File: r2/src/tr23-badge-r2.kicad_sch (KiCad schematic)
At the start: 60 parts, among them Q1 MMBT3904-TP, Q2 MMBT3904-TP, Q3 MMBT3904-TP, Y1 32.768kHz

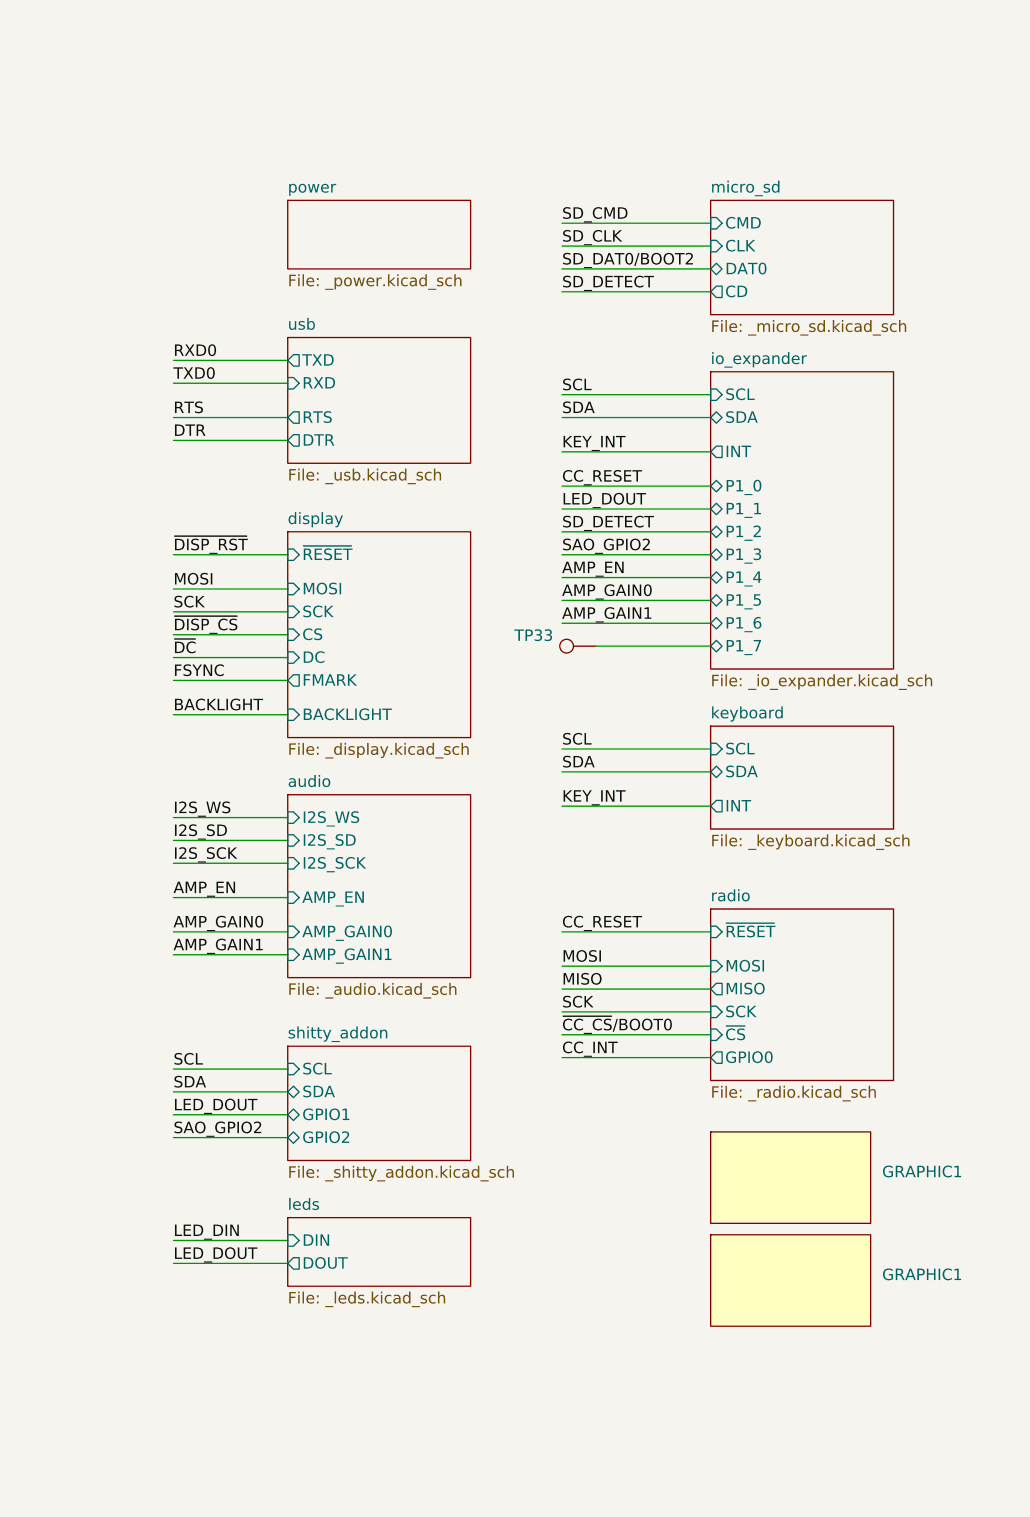
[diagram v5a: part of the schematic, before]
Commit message: Footprint reference for BSilk graphic
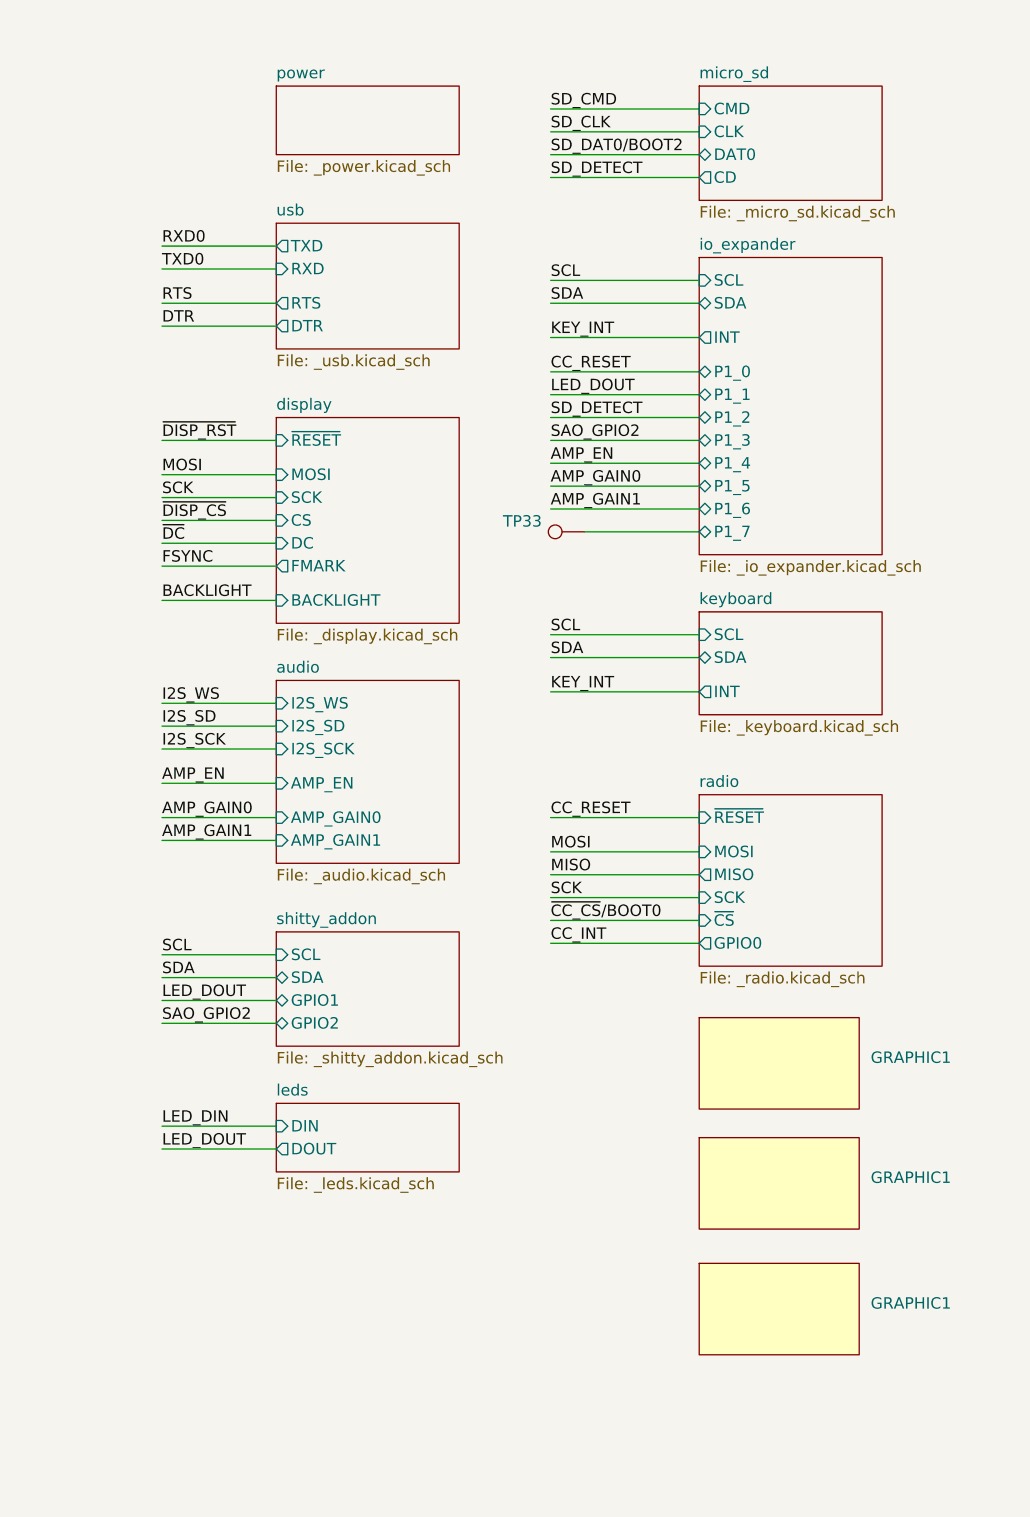
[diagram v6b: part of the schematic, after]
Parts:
- added GRAPHIC1: ~, tr23-svg2sz:tr23-r2-svg2sz-back, symbol j_Display:Display_dummy
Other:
- moved on the sheet: GRAPHIC1, TP33
